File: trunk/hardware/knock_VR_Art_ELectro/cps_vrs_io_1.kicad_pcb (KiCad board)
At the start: 2 copper layers, 41.9 x 30.5 mm, 38 parts, among them P1 CONN_2, P2 CONN_2, P3 CONN_5X2, P31 CONN_1, P32 CONN_1, P4 CONN_4, U20 MAX9926/9927, U24 MAX9939

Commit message: v 2
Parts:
- moved R44 13.7 mm to (212.2, 59.1)
- moved C6 3.26 mm to (217.9, 58.8)
- moved R52 2.99 mm to (214.4, 74.2), turned to 0 degrees
- moved R45 1.78 mm to (214.5, 59.1)
- moved R66 1.68 mm to (242.6, 60.5), turned to 180 degrees
- moved R62 1.17 mm to (231.6, 57.4)
- moved R49 0.91 mm to (217.9, 60.9)
- moved R43 0.55 mm to (209.9, 59.1)
- moved R37 0.48 mm to (207.9, 63.0)
- moved C10 0.42 mm to (227.0, 63.3)
- moved R42 0.18 mm to (225.7, 48.3)
- turned C33 to 180 degrees
- turned R48 to 270 degrees
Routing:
- net GND: track 82.8 -> 11.4 mm
- net /CAM: track 68.0 -> 36.6 mm, vias 2 -> 0
- net N-0000029: track 35.7 -> 10.5 mm
- net N-000004: track 33.9 -> 13.3 mm
- net 5V: track 66.1 -> 84.6 mm
- net /knock1-: track 35.0 -> 17.0 mm
- net N-0000022: track 13.2 -> 3.42 mm
- net /CAM+: track 18.2 -> 11.4 mm
- net N-0000026: track 15.9 -> 10.00 mm
- net /SCK: track 15.2 -> 11.2 mm, vias 0 -> 1
- net /CRANK: track 21.8 -> 25.1 mm
- net N-0000028: track 9.84 -> 12.7 mm
- net N-0000027: track 15.6 -> 17.7 mm
- net /FAKE-CAM: track 6.28 -> 7.84 mm
- net N-000002: track 7.67 -> 6.28 mm
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- added copper zone on F.Cu, net GND
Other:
- net class Default: clearance 0.254 -> 0.1
- rule trace_clearance: 0.254 -> 0.1

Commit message: with LED
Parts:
- added D1: LED, SM0805, F.Cu at (229.9, 49.5)
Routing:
- net N-0000014: track 5.25 -> 7.17 mm

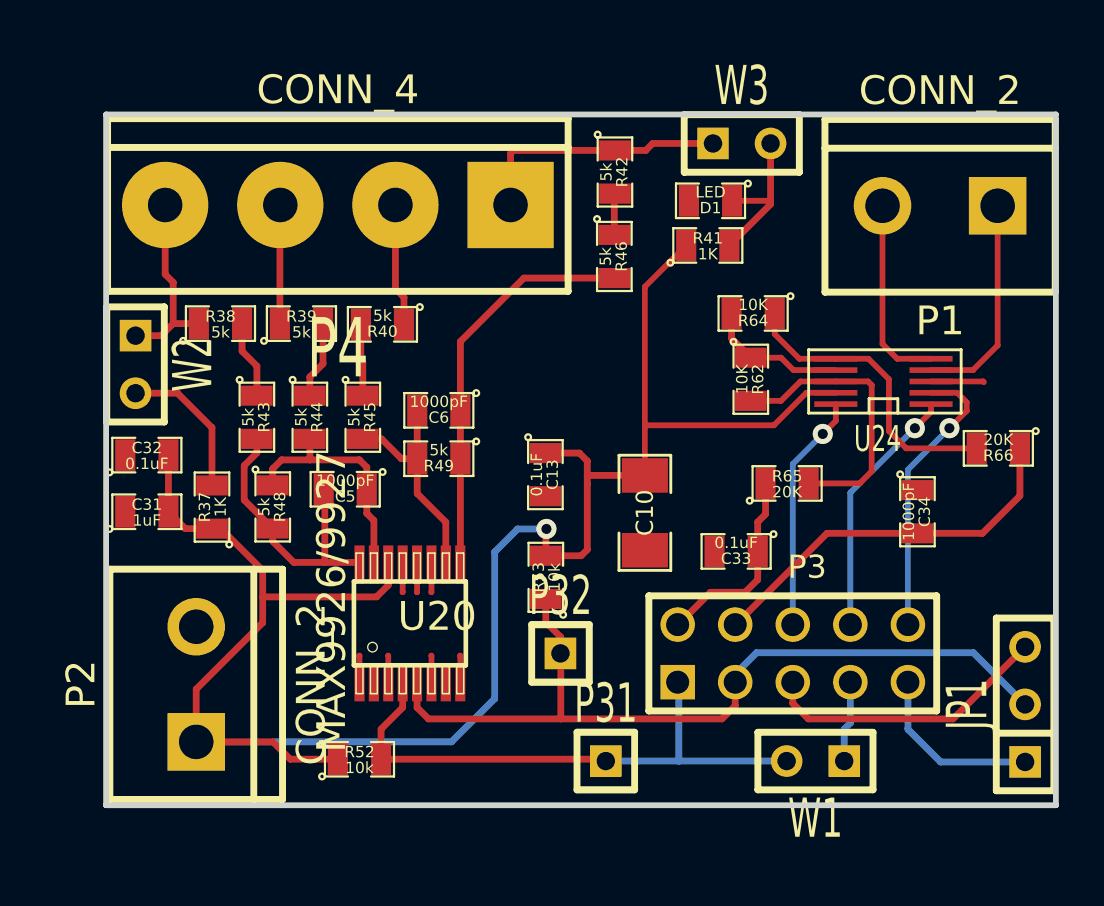
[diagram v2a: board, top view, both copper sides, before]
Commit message: 
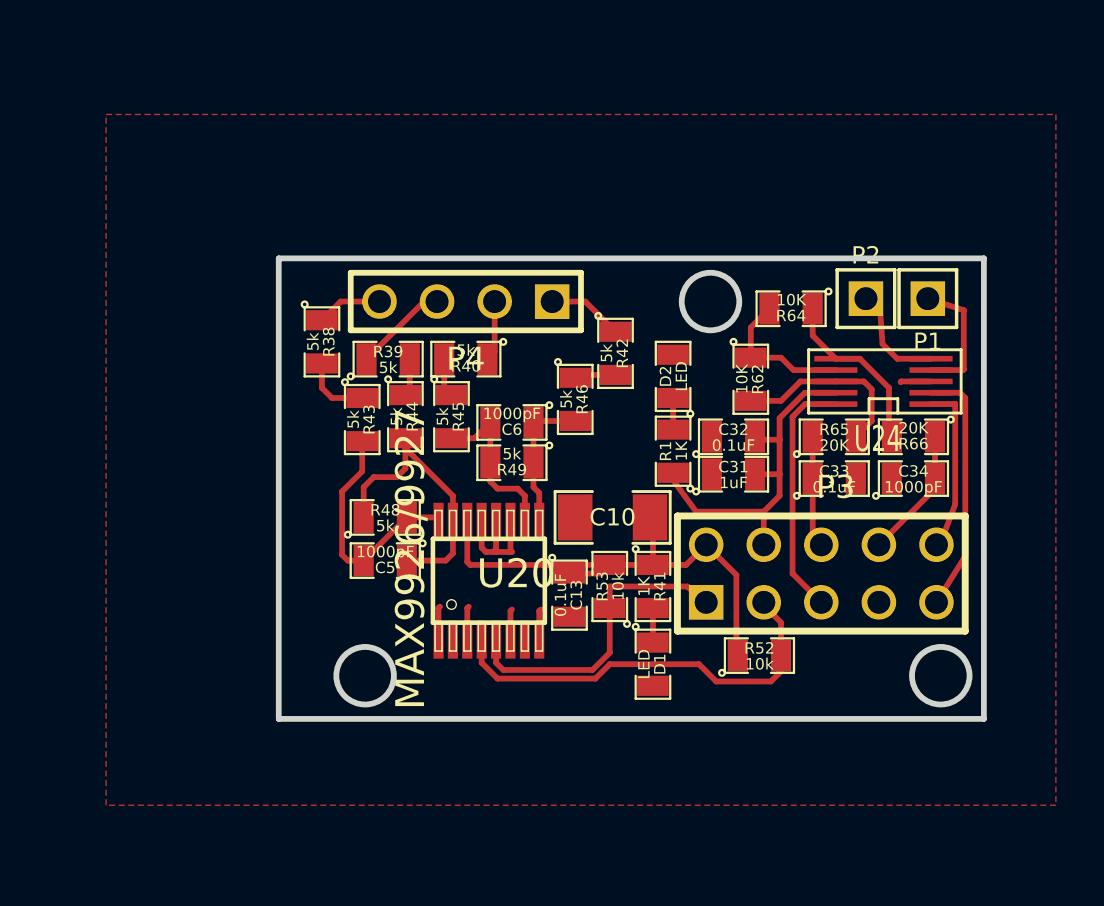
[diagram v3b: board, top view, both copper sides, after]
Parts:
- removed JP1: JUMPER3, SIL-3
- removed P31, P32: CONN_1, SIL-1
- removed R37: 1K, SM0805
- removed W1, W2, W3: JMP, SIL-2
- added D2: LED, SM0805, F.Cu at (228.2, 57.3)
- added R1: 1K, SM0805, F.Cu at (228.2, 60.6)
- P1, P2: value CONN_2 -> CONN_1; footprint bornier2 -> PIN_ARRAY_1
- P4: footprint bornier4 -> PIN_ARRAY_4x1
- moved P2 34.1 mm to (236.7, 53.8), turned to 0 degrees
- moved C31 25.9 mm to (230.9, 61.6)
- moved C32 25.9 mm to (230.9, 59.9)
- moved D1 20.6 mm to (227.3, 70.0), turned to 270 degrees
- moved R52 18.2 mm to (232.0, 69.6)
- moved R41 15.2 mm to (227.3, 66.5), turned to 270 degrees
- moved R42 8.00 mm to (225.7, 56.3)
- moved P4 7.07 mm to (219.1, 54.0)
- moved R46 6.54 mm to (223.9, 58.3)
- moved C13 5.42 mm to (223.6, 66.9)
- moved C33 5.39 mm to (235.3, 61.8), turned to 0 degrees
- moved R48 4.99 mm to (215.5, 63.5), turned to 0 degrees
- moved R43 4.65 mm to (214.5, 59.2)
- moved R38 4.55 mm to (212.7, 55.8), turned to 270 degrees
- moved R44 4.22 mm to (216.4, 59.1)
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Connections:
- net /CRK1+ renamed N-0000016
- C10 pad 2: 5V -> /5V
- C13 pad 1: 5V -> /5V
- C31 pad 2: 5V -> /5v stab
- C32 pad 2: 5V -> /5v stab
- P2 pad 1: 5V -> /knock_1+p
- P3 pad 1: /CRANK -> /CAM
- P3 pad 10: /MISO -> /SCK
- P3 pad 2: /knock1+ -> /5V
- P3 pad 3: /CAM -> /CRANK
- P3 pad 4: /knock1- -> /5v stab
- P3 pad 5: /RPMGEN_1 -> /CS-KN1
- P3 pad 6: /CS-KN1 -> /knock1+
- P3 pad 7: /RPMGEN_0 -> GND
- P3 pad 8: /SCK -> /knock1-
- P3 pad 9: /FAKE-CAM -> /MISO
- R41 pad 1: 5V -> /5V
- R52 pad 1: 5V -> /5V
- R53 pad 2: 5V -> /5V
- U20 pad 14: 5V -> /5V
- U24 pad 9: 5V -> /5v stab
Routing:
- net 5V: track 84.6 -> 0.00 mm, vias 1 -> 0
- net /5V: track 0.00 -> 23.8 mm
- net /CAM: track 36.6 -> 13.9 mm
- net /5v stab: track 0.00 -> 16.1 mm
- net /RPMGEN_1: track 12.8 -> 0.00 mm
- net N-0000031: track 17.7 -> 6.27 mm
- net /knock1-: track 17.0 -> 5.79 mm
- net /CAM+: track 11.4 -> 3.35 mm
- net /FAKE-CAM: track 7.84 -> 0.00 mm
- net N-0000015: track 6.55 -> 0.00 mm
- net /CRANK: track 25.1 -> 18.8 mm
- net N-0000013: track 7.17 -> 1.52 mm
- net N-0000016: track 8.40 -> 2.88 mm
- net N-0000011: track 13.3 -> 8.39 mm
- net N-000004: track 12.6 -> 8.22 mm
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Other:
- board size 41.9 x 30.5 mm -> 31.1 x 20.3 mm

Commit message: better layout
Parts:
- moved D2 3.74 mm to (226.1, 60.3), turned to 270 degrees
- moved R42 0.57 mm to (225.4, 56.8)
- moved P3 0.45 mm to (234.8, 65.5)
- moved R46 0.25 mm to (223.6, 58.3)
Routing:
- net N-0000014: track 1.40 -> 2.26 mm
- net /CAM+: track 3.35 -> 4.05 mm
- net /5V: track 23.8 -> 24.5 mm
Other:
- outline, holes or cut-outs redrawn

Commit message: better layout
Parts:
- moved R42 0.77 mm to (225.3, 56.0)
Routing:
- net /CAM+: track 4.05 -> 4.81 mm
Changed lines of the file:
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@@
   (general
     (links 67)
-    (no_connects 1)
+    (no_connects 0)
     (area 203.2 33.6931 263.733645 76.200001)
     (thickness 1.6)
     (drawings 11)
-    (tracks 172)
+    (tracks 174)
     (zones 0)
     (modules 34)
@@
   )
   (module SM0805 (layer F.Cu)
-    (at 225.425 56.769 270)
+    (at 225.298 56.007 270)
     (attr smd)
     (fp_text reference R42 (at 0 -0.3175 270) (layer F.SilkS)
@@
   (segment (start 229.616 66.802) (end 228.854 66.548) (width 0.254) (layer F.Cu) (net 3) (status 10))
   (segment (start 229.796 66.855) (end 229.743 66.802) (width 0.3) (layer B.Cu) (net 3) (status 30))
+  (segment (start 225.298 55.8165) (end 225.298 55.0545) (width 0.254) (layer F.Cu) (net 4))
   (segment (start 222.885 53.975) (end 222.885 55.245) (width 0.254) (layer F.Cu) (net 4))
-  (segment (start 223.4565 55.8165) (end 225.425 55.8165) (width 0.254) (layer F.Cu) (net 4))
+  (segment (start 223.4565 55.8165) (end 225.298 55.8165) (width 0.254) (layer F.Cu) (net 4))
+  (segment (start 225.298 55.8165) (end 225.425 55.8165) (width 0.254) (layer F.Cu) (net 4))
   (segment (start 222.885 55.245) (end 223.4565 55.8165) (width 0.254) (layer F.Cu) (net 4))
   (segment (start 220.345 53.975) (end 220.345 56.1975) (width 0.254) (layer F.Cu) (net 5) (status 30))
@@
   (segment (start 218.1225 56.515) (end 218.1225 57.785) (width 0.254) (layer F.Cu) (net 21) (status 30))
   (segment (start 218.1225 57.785) (end 218.44 58.1025) (width 0.254) (layer F.Cu) (net 21) (status 30))
-  (segment (start 225.425 57.7215) (end 224.028 57.7215) (width 0.254) (layer F.Cu) (net 22))
-  (segment (start 224.028 57.7215) (end 223.647 57.3405) (width 0.254) (layer F.Cu) (net 22))
+  (segment (start 223.647 57.3405) (end 224.917 57.3405) (width 0.254) (layer F.Cu) (net 22))
+  (segment (start 224.917 57.3405) (end 225.298 56.9595) (width 0.254) (layer F.Cu) (net 22))
   (segment (start 216.5985 56.515) (end 216.5985 57.912) (width 0.254) (layer F.Cu) (net 23) (status 30))
   (segment (start 216.5985 57.912) (end 216.408 58.1025) (width 0.254) (layer F.Cu) (net 23) (status 30))

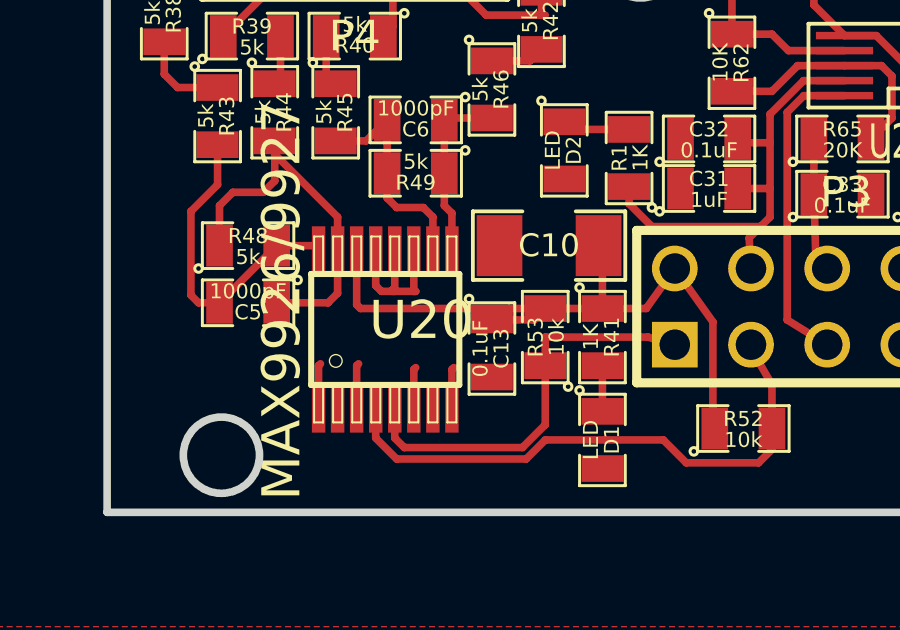
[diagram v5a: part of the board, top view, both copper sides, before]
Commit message: the logo finally works
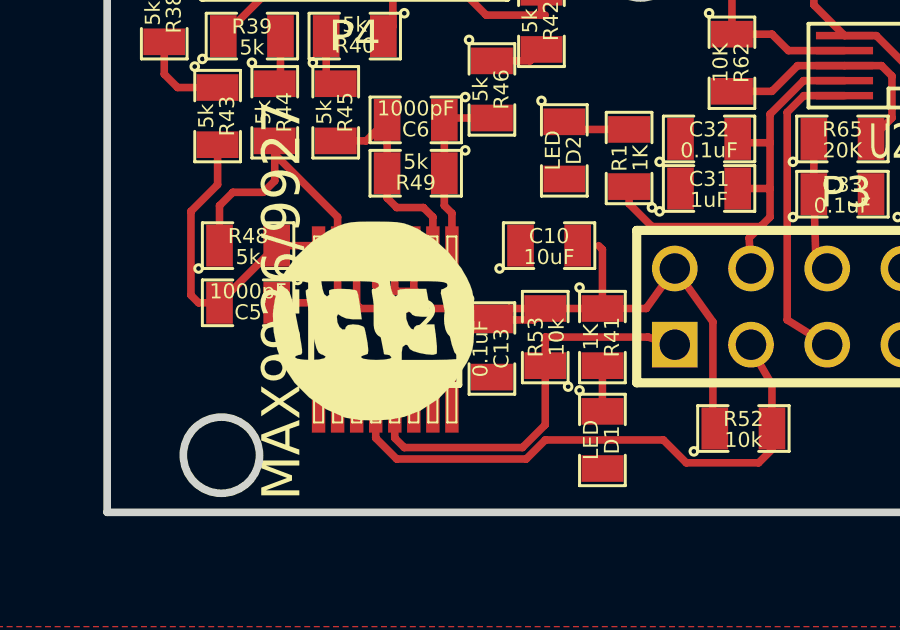
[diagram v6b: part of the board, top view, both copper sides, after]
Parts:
- added G1: LOGO, LOGO_F, F.Cu at (219.7, 66.0)
- C10: footprint SM1206 -> SM0805
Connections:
- U20 pad 2: N-0000024 -> (no net)
- U20 pad 7: N-0000025 -> (no net)

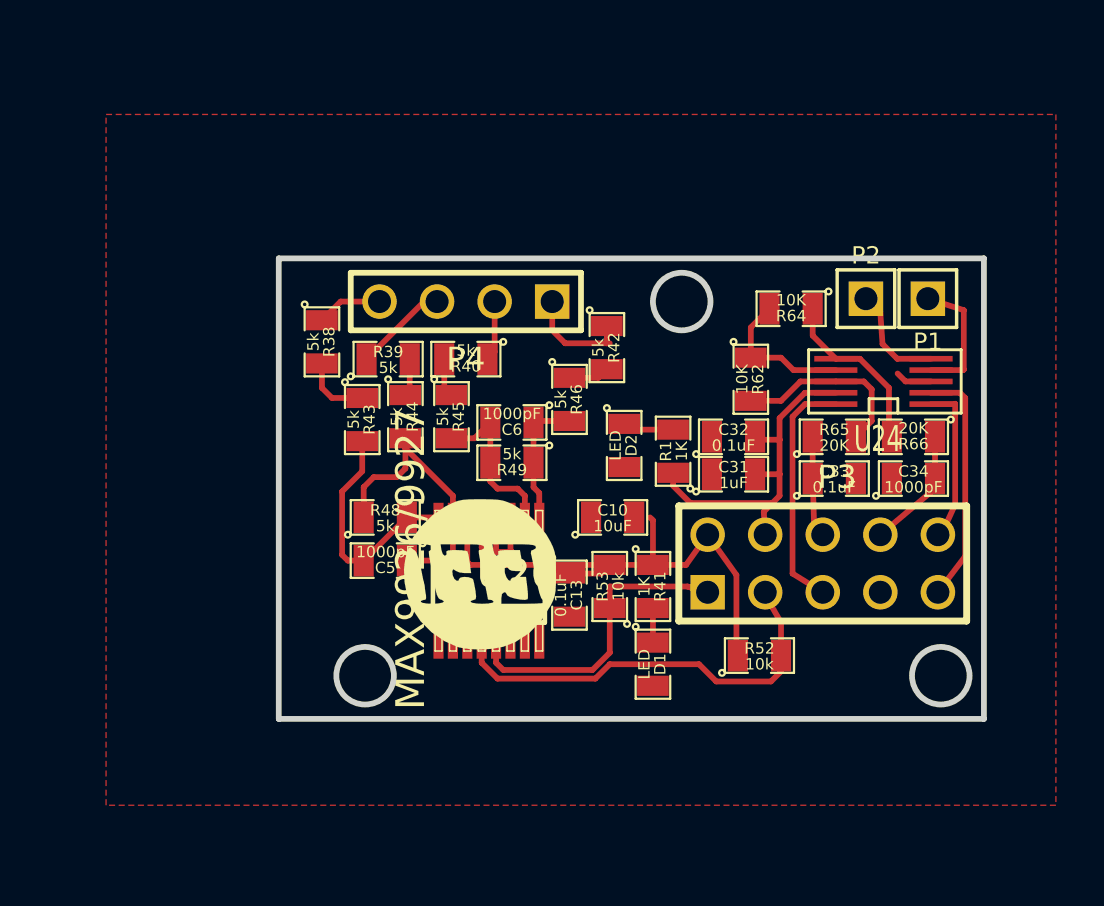
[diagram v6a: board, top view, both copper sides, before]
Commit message: 
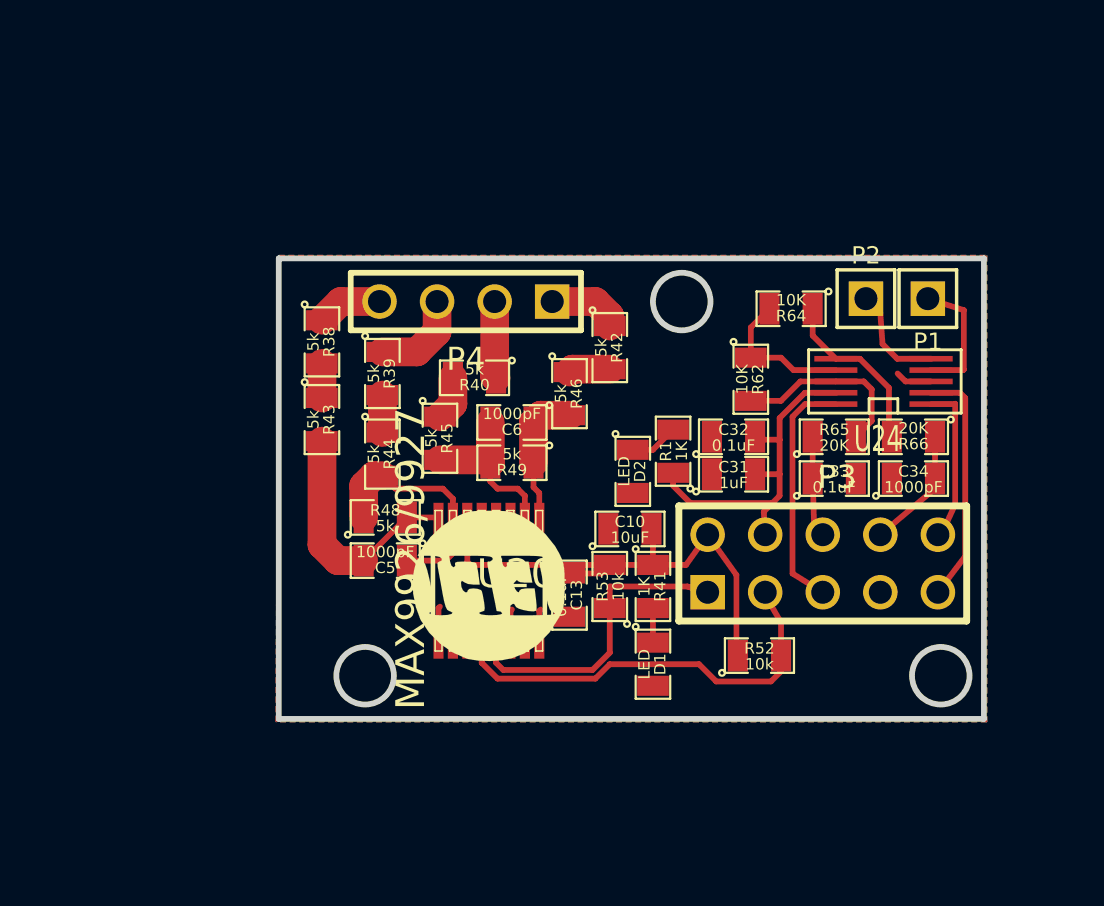
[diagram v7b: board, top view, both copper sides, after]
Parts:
- moved R44 1.94 mm to (215.4, 60.7)
- moved R43 1.78 mm to (212.7, 59.2)
- moved D2 1.20 mm to (226.4, 61.5)
- moved R45 1.08 mm to (217.9, 60.0)
- moved C10 0.92 mm to (226.3, 64.0)
- moved R40 0.91 mm to (219.5, 57.3)
- moved R39 0.68 mm to (215.4, 57.1), turned to 270 degrees
- moved G1 0.63 mm to (220.1, 66.5)
- moved R46 0.25 mm to (223.6, 58.0)
- moved R42 0.13 mm to (225.4, 56.0)
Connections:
- net N-0000016 renamed /CRK2+
- U20 pad 2: (no net) -> N-0000023
- U20 pad 7: (no net) -> N-0000024
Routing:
- net N-0000028: track 13.0 -> 10.5 mm
- net /CAM+: track 4.81 -> 3.25 mm
- net N-0000017: track 3.04 -> 1.52 mm
- net /CAM-: track 2.67 -> 3.39 mm
- net /5V: track 24.5 -> 23.9 mm
- net /CRK2-: track 4.16 -> 4.69 mm
- added copper zone on B.Cu, net GND
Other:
- net class VR added: clearance 0.4, trace_width 1.27, via_dia 0.889, via_drill 0.635
